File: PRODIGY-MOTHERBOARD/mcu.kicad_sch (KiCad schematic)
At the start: 19 parts, among them J1 USB_C_Receptacle, J2 Bus_M.2_Socket_B, SW1 SW_Push

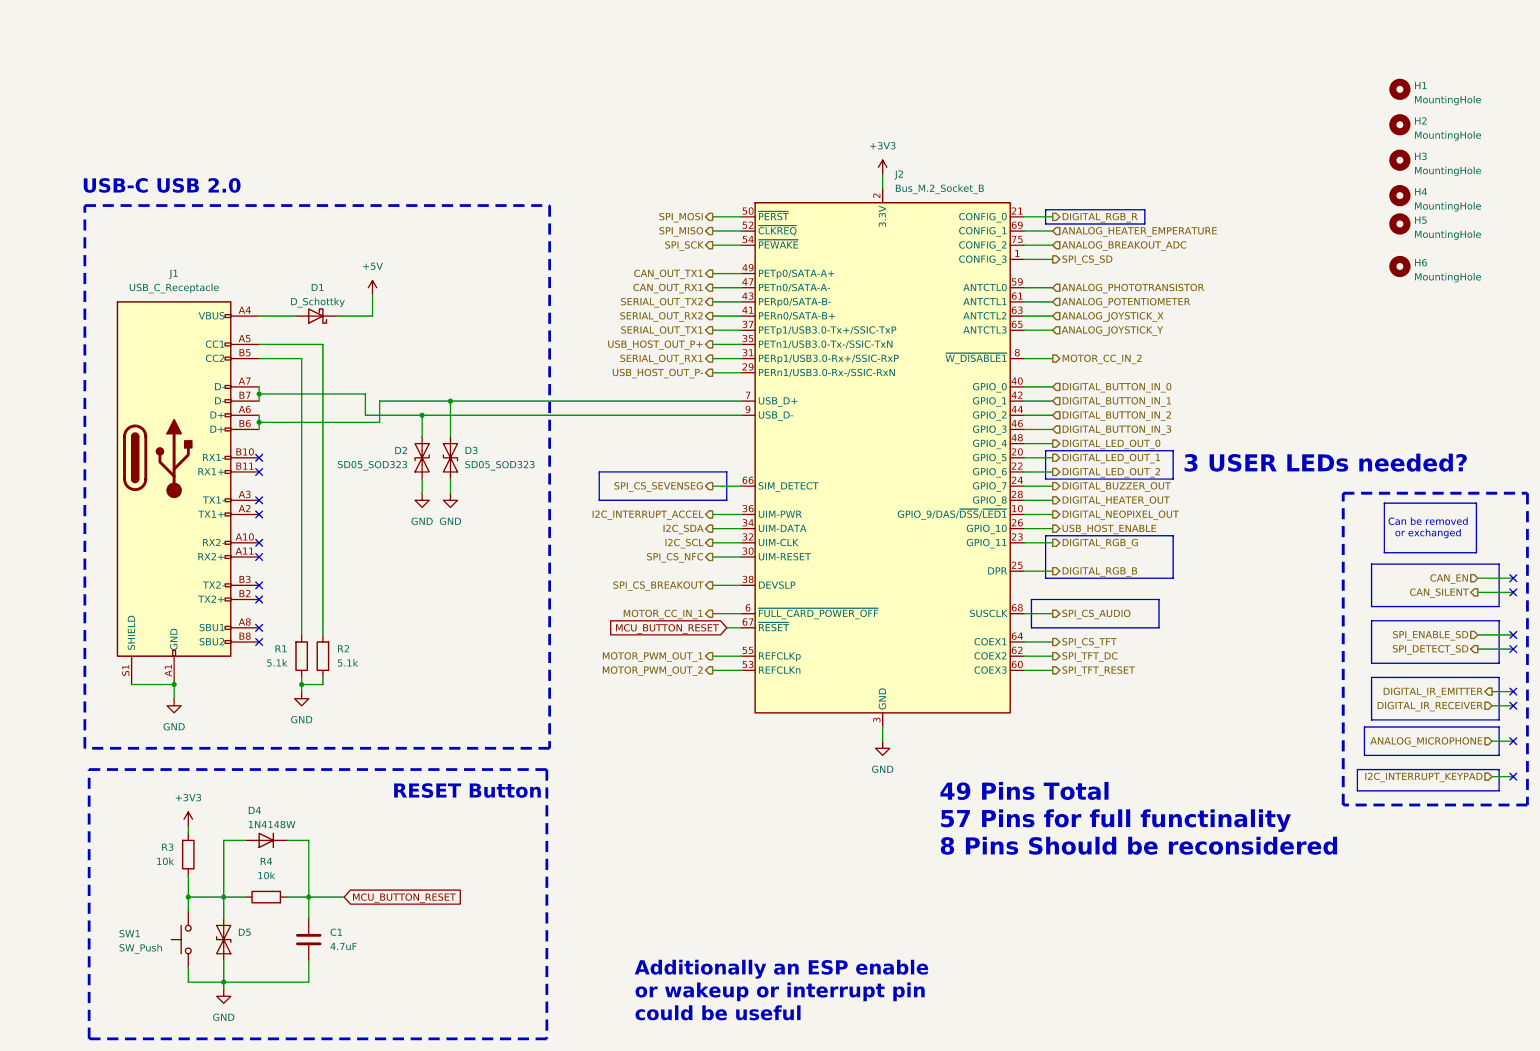
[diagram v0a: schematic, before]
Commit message: MCU schematic done. Started Analog design.
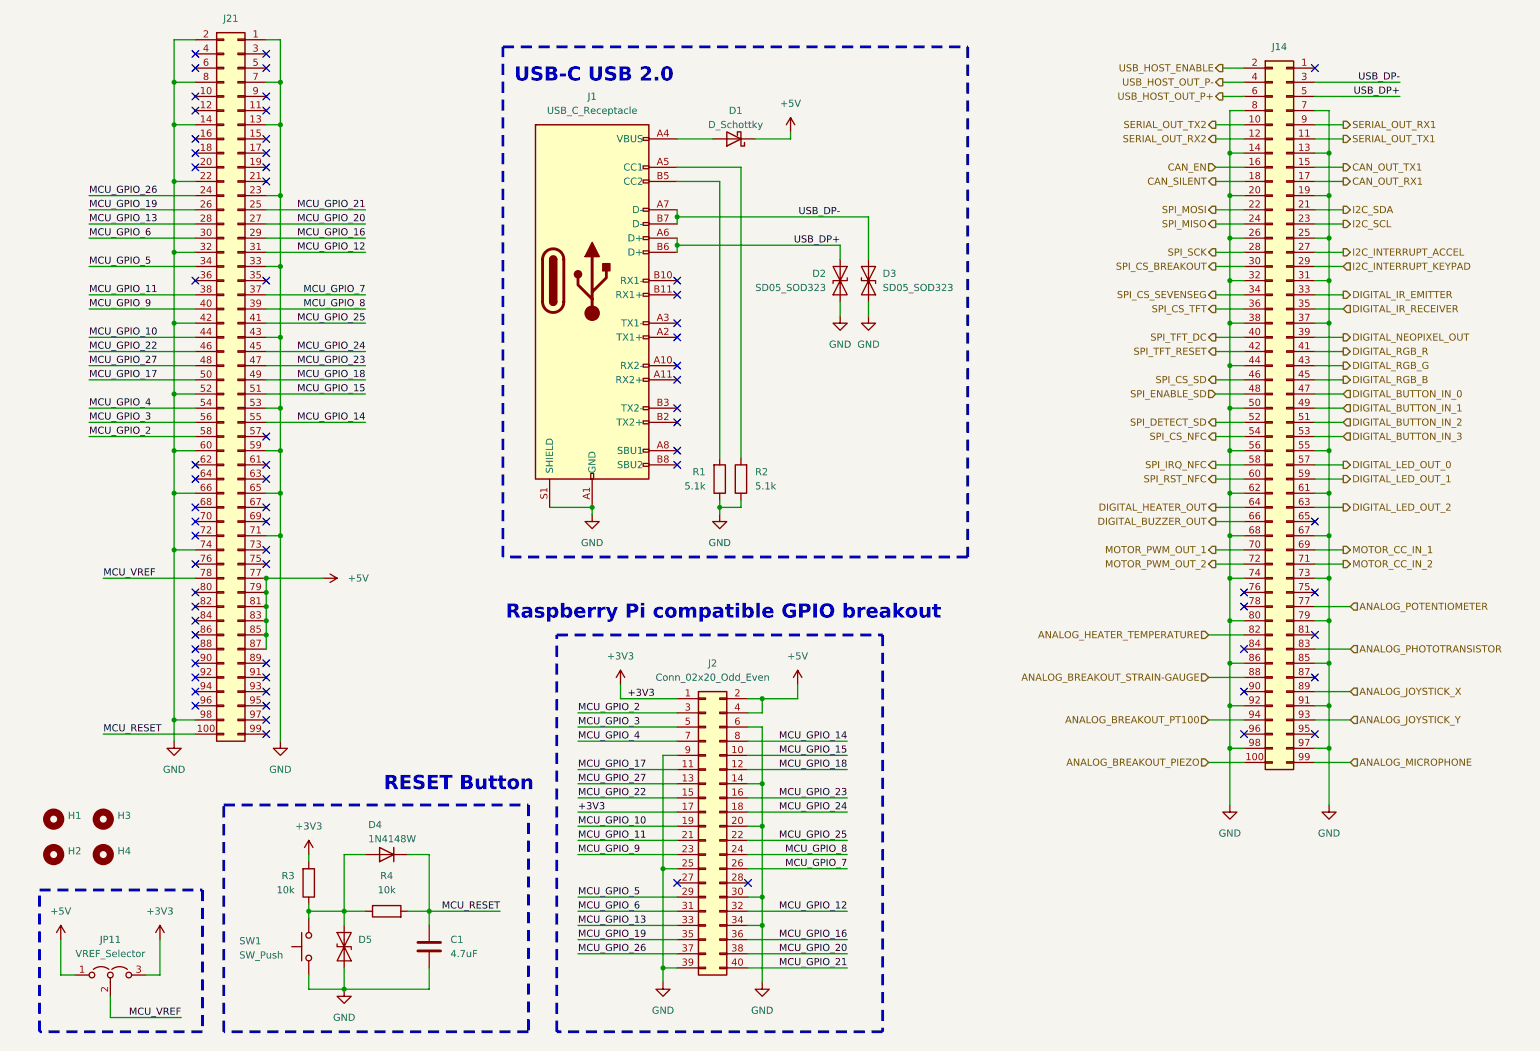
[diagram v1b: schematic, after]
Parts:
- removed H5, H6: MountingHole, MountingHole:MountingHole_3.2mm_M3_ISO7380_Pad_TopBottom, symbol Mechanical:MountingHole
- removed J2: Bus_M.2_Socket_B, symbol Connector:Bus_M.2_Socket_B
- added J14, J21: ~, symbol 2x50_generic_connector:2x50_Odd-Even
- added J2: Conn_02x20_Odd_Even, Connector_PinHeader_2.54mm:PinHeader_2x20_P2.54mm_Horizontal, symbol Connector_Generic:Conn_02x20_Odd_Even
- added JP11: VREF_Selector, symbol Jumper:Jumper_3_Open
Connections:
- net +3V3: now also J2.1 (Pin_1), J2.17 (Pin_17), JP11.3 (B)
- net +5V: now also J2.2 (Pin_2), J2.4 (Pin_4), J21.77, J21.79, J21.81, J21.83, J21.85, J21.87, JP11.1 (A)
- net ANALOG_JOYSTICK_X: now also J14.89
- net ANALOG_JOYSTICK_Y: now also J14.93
- net ANALOG_MICROPHONE: now also J14.99
- net ANALOG_PHOTOTRANSISTOR: now also J14.83
- net ANALOG_POTENTIOMETER: now also J14.77
- net CAN_EN: now also J14.16
- net CAN_OUT_RX1: now also J14.17
- net CAN_OUT_TX1: now also J14.15
- net CAN_SILENT: now also J14.18
- net DIGITAL_BUTTON_IN_0: now also J14.47
- net DIGITAL_BUTTON_IN_1: now also J14.49
- net DIGITAL_BUTTON_IN_2: now also J14.51
- net DIGITAL_BUTTON_IN_3: now also J14.53
- net DIGITAL_BUZZER_OUT: now also J14.66
- net DIGITAL_HEATER_OUT: now also J14.64
- net DIGITAL_IR_EMITTER: now also J14.33
- net DIGITAL_IR_RECEIVER: now also J14.35
- net DIGITAL_LED_OUT_0: now also J14.57
- net DIGITAL_LED_OUT_1: now also J14.59
- net DIGITAL_LED_OUT_2: now also J14.63
- net DIGITAL_NEOPIXEL_OUT: now also J14.39
- net DIGITAL_RGB_B: now also J14.45
- net DIGITAL_RGB_G: now also J14.43
- net DIGITAL_RGB_R: now also J14.41
- net GND: now also J14.13, J14.14, J14.19, J14.20, J14.25, J14.26, J14.31, J14.32, J14.37, J14.38, J14.44, J14.50, J14.55, J14.56, J14.61, J14.62, J14.67, J14.68, J14.7, J14.73, J14.74, J14.79, J14.8, J14.80, J14.85, J14.86, J14.91, J14.92, J14.97, J14.98, J2.14 (Pin_14), J2.20 (Pin_20), J2.25 (Pin_25), J2.30 (Pin_30), J2.34 (Pin_34), J2.39 (Pin_39), J2.6 (Pin_6), J2.9 (Pin_9), J21.1, J21.13, J21.14, J21.2, J21.22, J21.23, J21.32, J21.33, J21.42, J21.43, J21.52, J21.53, J21.59, J21.60, J21.65, J21.66, J21.7, J21.71, J21.74, J21.8, J21.98
- net I2C_INTERRUPT_ACCEL: now also J14.27
- net I2C_INTERRUPT_KEYPAD: now also J14.29
- net I2C_SCL: now also J14.23
- net I2C_SDA: now also J14.21
- net MOTOR_CC_IN_1: now also J14.69
- net MOTOR_CC_IN_2: now also J14.71
- net MOTOR_PWM_OUT_1: now also J14.70
- net MOTOR_PWM_OUT_2: now also J14.72
- net SERIAL_OUT_RX1: now also J14.9
- net SERIAL_OUT_RX2: now also J14.12
- net SERIAL_OUT_TX1: now also J14.11
- net SERIAL_OUT_TX2: now also J14.10
- net SPI_CS_BREAKOUT: now also J14.30
- net SPI_CS_NFC: now also J14.54
- net SPI_CS_SD: now also J14.46
- net SPI_CS_SEVENSEG: now also J14.34
- net SPI_CS_TFT: now also J14.36
- net SPI_DETECT_SD: now also J14.52
- net SPI_ENABLE_SD: now also J14.48
- net SPI_MISO: now also J14.24
- net SPI_MOSI: now also J14.22
- net SPI_SCK: now also J14.28
- net SPI_TFT_DC: now also J14.40
- net SPI_TFT_RESET: now also J14.42
- net USB_HOST_ENABLE: now also J14.2
- net USB_HOST_OUT_P+: now also J14.6
- net USB_HOST_OUT_P-: now also J14.4
- net USB_DP-: now reaches J1.A7 (D-), J1.B7 (D-)
- net USB_DP-: now also D3.2 (A2), J14.3; no longer D2.2 (A2)
- net USB_DP+: now reaches J1.A6 (D+), J1.B6 (D+)
- net USB_DP+: now also D2.2 (A2), J14.5; no longer D3.2 (A2)
- net MCU_BUTTON_RESET renamed MCU_RESET
- net MCU_RESET: now also J21.100
- new net ANALOG_BREAKOUT_PIEZO: J14.100
- new net ANALOG_BREAKOUT_PT100: J14.94
- new net ANALOG_BREAKOUT_STRAIN-GAUGE: J14.88
- new net ANALOG_HEATER_TEMPERATURE: J14.82
- new net MCU_GPIO_10: J2.19 (Pin_19), J21.44
- new net MCU_GPIO_11: J2.21 (Pin_21), J21.38
- new net MCU_GPIO_12: J2.32 (Pin_32), J21.31
- new net MCU_GPIO_13: J2.33 (Pin_33), J21.28
- new net MCU_GPIO_14: J2.8 (Pin_8), J21.55
- new net MCU_GPIO_15: J2.10 (Pin_10), J21.51
- new net MCU_GPIO_16: J2.36 (Pin_36), J21.29
- new net MCU_GPIO_17: J2.11 (Pin_11), J21.50
- new net MCU_GPIO_18: J2.12 (Pin_12), J21.49
- new net MCU_GPIO_19: J2.35 (Pin_35), J21.26
- new net MCU_GPIO_2: J2.3 (Pin_3), J21.58
- new net MCU_GPIO_20: J2.38 (Pin_38), J21.27
- new net MCU_GPIO_21: J2.40 (Pin_40), J21.25
- new net MCU_GPIO_22: J2.15 (Pin_15), J21.46
- new net MCU_GPIO_23: J2.16 (Pin_16), J21.47
- new net MCU_GPIO_24: J2.18 (Pin_18), J21.45
- new net MCU_GPIO_25: J2.22 (Pin_22), J21.41
- new net MCU_GPIO_26: J2.37 (Pin_37), J21.24
- new net MCU_GPIO_27: J2.13 (Pin_13), J21.48
- new net MCU_GPIO_3: J2.5 (Pin_5), J21.56
- new net MCU_GPIO_4: J2.7 (Pin_7), J21.54
- new net MCU_GPIO_5: J2.29 (Pin_29), J21.34
- new net MCU_GPIO_6: J2.31 (Pin_31), J21.30
- new net MCU_GPIO_7: J2.26 (Pin_26), J21.37
- new net MCU_GPIO_8: J2.24 (Pin_24), J21.39
- new net MCU_GPIO_9: J2.23 (Pin_23), J21.40
- new net MCU_VREF: J21.78, JP11.2 (C)
- new net SPI_IRQ_NFC: J14.58
- new net SPI_RST_NFC: J14.60
- no-connect marks 18 -> 68
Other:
- note added: "Raspberry Pi compatible GPIO breakout"
- note removed: "3 USER LEDs needed?"
- note removed: "49 Pins Total 57 Pins for full functinality 8 Pins Should be reconsidered"
- note removed: "Additionally an ESP enable or wakeup or interrupt pin could be useful"
- note removed: "Can be removed or exchanged"
- moved on the sheet: C1, D1, D2, D3, D4, D5, H1, J1, R1, R2, R3, R4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

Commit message: Finished v0.1 schematic.
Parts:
- removed H1, H2, H3, H4: MountingHole, MountingHole:MountingHole_3.2mm_M3_ISO7380_Pad_TopBottom, symbol Mechanical:MountingHole
- added FID7, FID8: Fiducial, symbol Mechanical:Fiducial
- added H5, H6, H7, H8: MountingHole, MountingHole:MountingHole_3.2mm_M3_ISO7380_Pad_TopBottom, symbol Mechanical:MountingHole
- J1: renamed from J21; value ~ -> DF40C-100DS-0.4V(51)
- J2: renamed from J1; footprint (none) -> Connector_USB:USB_C_Receptacle_G-Switch_GT-USB-7025
- J4: renamed from J14; value ~ -> DF40C-100DS-0.4V(51)
- renumbered D5 to D1, D4 to D2, D1 to D3, D2 to D4, D3 to D5, J2 to J3, JP11 to JP1, R3 to R1, R4 to R2, R1 to R3, R2 to R4
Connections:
- net ANALOG_BREAKOUT_STRAIN-GAUGE is gone; now on net ANALOG_HEATER_TEMPERATURE: J4.88
- net ANALOG_HEATER_TEMPERATURE: no longer J4.82
- net ANALOG_JOYSTICK_X: now also J4.87; no longer J4.89
- net ANALOG_PHOTOTRANSISTOR: now also J4.81; no longer J4.83
- net ANALOG_POTENTIOMETER: now also J4.82; no longer J4.77
- no-connect marks 68 -> 69
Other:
- moved on the sheet: J1, JP1

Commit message: MBT Schematic improved
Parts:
- added JP12: Vout_select, symbol Jumper:Jumper_3_Bridged12
- added TP15: ~, TestPoint:TestPoint_Pad_D3.0mm, symbol Connector:TestPoint
- J3: footprint Connector_PinHeader_2.54mm:PinHeader_2x20_P2.54mm_Horizontal -> Connector_IDC:IDC-Header_2x20_P2.54mm_Horizontal
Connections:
- net SPI_CS_SD is gone; now on net SPI_CS_NFC: J4.46
- net SPI_DETECT_SD is gone; now on net SPI_RST_NFC: J4.52
- net SPI_ENABLE_SD is gone; now on net SPI_IRQ_NFC: J4.48
- net +3V3: now also J1.84, J1.86, JP12.1 (A)
- net DIGITAL_BUZZER_OUT: now also J4.60; no longer J4.66
- net DIGITAL_HEATER_OUT: now also J4.54; no longer J4.64
- net DIGITAL_LED_OUT_2: now also J4.58; no longer J4.63
- net MCU_VREF: now also TP15.1
- net MOTOR_CC_IN_1: now also J4.65; no longer J4.69
- net MOTOR_CC_IN_2: now also J4.66; no longer J4.71
- net MOTOR_PWM_OUT_1: now also J4.63; no longer J4.70
- net MOTOR_PWM_OUT_2: now also J4.64; no longer J4.72
- net SPI_CS_NFC: no longer J4.54
- net SPI_IRQ_NFC: no longer J4.58
- net SPI_RST_NFC: no longer J4.60
- net SD_CLK: now reaches J1.57
- net SD_DAT3: now reaches J1.61
- net SD_CMD: now reaches J1.62
- net SD_DAT0: now reaches J1.63
- net SD_DAT1: now reaches J1.67
- net SD_DAT2: now reaches J1.69
- net SD_Enable: now reaches J1.75
- net SD_DET: now reaches J1.76
- net at J1.88: now also J1.90, JP12.2 (C)
- net USB_HOST_FAULT: now reaches J4.1
- new net +1V8: JP12.3 (B)
- no-connect marks 69 -> 59
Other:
- moved on the sheet: J1

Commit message: schematic v0.2 finalized
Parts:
- renumbered H5 to H6, H6 to H7, H7 to H8, H8 to H9, JP12 to JP2, TP15 to TP1
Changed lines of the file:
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@@
 		(dnp no)
 		(fields_autoplaced yes)
-		(property "Reference" "H8"
+		(property "Reference" "H9"
 			(at 41.91 165.735 0)
 			(effects
@@
 			(project "PRODIGY-MOTHERBOARD"
 				(path "/f1c25860-8989-4190-bd24-2491d23ca7d9/27fc7bb4-2bbd-477b-b6e3-e07582947566"
-					(reference "H8")
+					(reference "H9")
 					(unit 1)
 				)
@@
 		(dnp no)
 		(fields_autoplaced yes)
-		(property "Reference" "H7"
+		(property "Reference" "H8"
 			(at 41.91 159.385 0)
 			(effects
@@
 			(project "PRODIGY-MOTHERBOARD"
 				(path "/f1c25860-8989-4190-bd24-2491d23ca7d9/27fc7bb4-2bbd-477b-b6e3-e07582947566"
-					(reference "H7")
+					(reference "H8")
 					(unit 1)
 				)
@@
 		(dnp no)
 		(fields_autoplaced yes)
-		(property "Reference" "#PWR014"
+		(property "Reference" "#PWR016"
 			(at 151.13 137.16 0)
 			(effects
@@
 			(project "PRODIGY-MOTHERBOARD"
 				(path "/f1c25860-8989-4190-bd24-2491d23ca7d9/27fc7bb4-2bbd-477b-b6e3-e07582947566"
-					(reference "#PWR014")
+					(reference "#PWR016")
 					(unit 1)
 				)
@@
 		(on_board yes)
 		(dnp no)
-		(property "Reference" "#PWR06"
+		(property "Reference" "#PWR08"
 			(at 66.04 116.84 0)
 			(effects
@@
 			(project "PRODIGY-MOTHERBOARD"
 				(path "/f1c25860-8989-4190-bd24-2491d23ca7d9/27fc7bb4-2bbd-477b-b6e3-e07582947566"
-					(reference "#PWR06")
+					(reference "#PWR08")
 					(unit 1)
 				)
@@
 		(dnp no)
 		(fields_autoplaced yes)
-		(property "Reference" "#PWR012"
+		(property "Reference" "#PWR014"
 			(at 144.78 193.04 0)
 			(effects
@@
 			(project "PRODIGY-MOTHERBOARD"
 				(path "/f1c25860-8989-4190-bd24-2491d23ca7d9/27fc7bb4-2bbd-477b-b6e3-e07582947566"
-					(reference "#PWR012")
+					(reference "#PWR014")
 					(unit 1)
 				)
@@
 		(dnp no)
 		(fields_autoplaced yes)
-		(property "Reference" "#PWR09"
+		(property "Reference" "#PWR011"
 			(at 119.38 137.16 0)
 			(effects
@@
 			(project "PRODIGY-MOTHERBOARD"
 				(path "/f1c25860-8989-4190-bd24-2491d23ca7d9/27fc7bb4-2bbd-477b-b6e3-e07582947566"
-					(reference "#PWR09")
+					(reference "#PWR011")
 					(unit 1)
 				)
@@
 		(dnp no)
 		(fields_autoplaced yes)
-		(property "Reference" "#PWR0248"
+		(property "Reference" "#PWR02"
 			(at 34.29 124.46 0)
 			(effects
@@
 			(project "PRODIGY-MOTHERBOARD"
 				(path "/f1c25860-8989-4190-bd24-2491d23ca7d9/27fc7bb4-2bbd-477b-b6e3-e07582947566"
-					(reference "#PWR0248")
+					(reference "#PWR02")
 					(unit 1)
 				)
@@
 		(dnp no)
 		(fields_autoplaced yes)
-		(property "Reference" "H6"
+		(property "Reference" "H7"
 			(at 33.02 165.735 0)
 			(effects
@@
 			(project "PRODIGY-MOTHERBOARD"
 				(path "/f1c25860-8989-4190-bd24-2491d23ca7d9/27fc7bb4-2bbd-477b-b6e3-e07582947566"
-					(reference "H6")
+					(reference "H7")
 					(unit 1)
 				)
@@
 		(dnp no)
 		(fields_autoplaced yes)
-		(property "Reference" "#PWR015"
+		(property "Reference" "#PWR017"
 			(at 158.75 73.66 0)
 			(effects
@@
 			(project "PRODIGY-MOTHERBOARD"
 				(path "/f1c25860-8989-4190-bd24-2491d23ca7d9/27fc7bb4-2bbd-477b-b6e3-e07582947566"
-					(reference "#PWR015")
+					(reference "#PWR017")
 					(unit 1)
 				)
@@
 		(dnp no)
 		(fields_autoplaced yes)
-		(property "Reference" "#PWR016"
+		(property "Reference" "#PWR018"
 			(at 163.83 73.66 0)
 			(effects
@@
 			(project "PRODIGY-MOTHERBOARD"
 				(path "/f1c25860-8989-4190-bd24-2491d23ca7d9/27fc7bb4-2bbd-477b-b6e3-e07582947566"
-					(reference "#PWR016")
+					(reference "#PWR018")
 					(unit 1)
 				)
@@
 		(dnp no)
 		(fields_autoplaced yes)
-		(property "Reference" "#PWR07"
+		(property "Reference" "#PWR09"
 			(at 69.85 194.31 0)
 			(effects
@@
 			(project "PRODIGY-MOTHERBOARD"
 				(path "/f1c25860-8989-4190-bd24-2491d23ca7d9/27fc7bb4-2bbd-477b-b6e3-e07582947566"
-					(reference "#PWR07")
+					(reference "#PWR09")
 					(unit 1)
 				)
@@
 		(dnp no)
 		(fields_autoplaced yes)
-		(property "Reference" "#PWR011"
+		(property "Reference" "#PWR013"
 			(at 137.16 109.22 0)
 			(effects
@@
 			(project "PRODIGY-MOTHERBOARD"
 				(path "/f1c25860-8989-4190-bd24-2491d23ca7d9/27fc7bb4-2bbd-477b-b6e3-e07582947566"
-					(reference "#PWR011")
+					(reference "#PWR013")
 					(unit 1)
 				)
@@
 		(dnp no)
 		(fields_autoplaced yes)
-		(property "Reference" "#PWR010"
+		(property "Reference" "#PWR012"
 			(at 127 193.04 0)
 			(effects
@@
 			(project "PRODIGY-MOTHERBOARD"
 				(path "/f1c25860-8989-4190-bd24-2491d23ca7d9/27fc7bb4-2bbd-477b-b6e3-e07582947566"
-					(reference "#PWR010")
+					(reference "#PWR012")
 					(unit 1)
 				)
@@
 		(dnp no)
 		(fields_autoplaced yes)
-		(property "Reference" "#PWR05"
+		(property "Reference" "#PWR07"
 			(at 63.5 167.64 0)
 			(effects
@@
 			(project "PRODIGY-MOTHERBOARD"
 				(path "/f1c25860-8989-4190-bd24-2491d23ca7d9/27fc7bb4-2bbd-477b-b6e3-e07582947566"
-					(reference "#PWR05")
+					(reference "#PWR07")
 					(unit 1)
 				)
@@
 		(dnp no)
 		(fields_autoplaced yes)
-		(property "Reference" "#PWR08"
+		(property "Reference" "#PWR010"
 			(at 114.3 109.22 0)
 			(effects
@@
 			(project "PRODIGY-MOTHERBOARD"
 				(path "/f1c25860-8989-4190-bd24-2491d23ca7d9/27fc7bb4-2bbd-477b-b6e3-e07582947566"
-					(reference "#PWR08")
+					(reference "#PWR010")
 					(unit 1)
 				)
@@
 		(dnp no)
 		(fields_autoplaced yes)
-		(property "Reference" "JP12"
+		(property "Reference" "JP2"
 			(at 29.21 129.5399 90)
 			(effects
@@
 			(project ""
 				(path "/f1c25860-8989-4190-bd24-2491d23ca7d9/27fc7bb4-2bbd-477b-b6e3-e07582947566"
-					(reference "JP12")
+					(reference "JP2")
 					(unit 1)
 				)
@@
 		(dnp no)
 		(fields_autoplaced yes)
-		(property "Reference" "H5"
+		(property "Reference" "H6"
 			(at 33.02 159.385 0)
 			(effects
@@
 			(project "PRODIGY-MOTHERBOARD"
 				(path "/f1c25860-8989-4190-bd24-2491d23ca7d9/27fc7bb4-2bbd-477b-b6e3-e07582947566"
-					(reference "H5")
+					(reference "H6")
 					(unit 1)
 				)
@@
 		(dnp no)
 		(fields_autoplaced yes)
-		(property "Reference" "#PWR03"
+		(property "Reference" "#PWR05"
 			(at 43.18 152.4 0)
 			(effects
@@
 			(project "PRODIGY-MOTHERBOARD"
 				(path "/f1c25860-8989-4190-bd24-2491d23ca7d9/27fc7bb4-2bbd-477b-b6e3-e07582947566"
-					(reference "#PWR03")
+					(reference "#PWR05")
 					(unit 1)
 				)
@@
 		(dnp no)
 		(fields_autoplaced yes)
-		(property "Reference" "#PWR018"
+		(property "Reference" "#PWR020"
 			(at 246.38 161.29 0)
 			(effects
@@
 			(project "PRODIGY-MOTHERBOARD"
 				(path "/f1c25860-8989-4190-bd24-2491d23ca7d9/27fc7bb4-2bbd-477b-b6e3-e07582947566"
-					(reference "#PWR018")
+					(reference "#PWR020")
 					(unit 1)
 				)
@@
 		(dnp no)
 		(fields_autoplaced yes)
-		(property "Reference" "#PWR04"
+		(property "Reference" "#PWR06"
 			(at 62.23 152.4 0)
 			(effects
@@
 			(project "PRODIGY-MOTHERBOARD"
 				(path "/f1c25860-8989-4190-bd24-2491d23ca7d9/27fc7bb4-2bbd-477b-b6e3-e07582947566"
-					(reference "#PWR04")
+					(reference "#PWR06")
 					(unit 1)
 				)
@@
 		(dnp no)
 		(fields_autoplaced yes)
-		(property "Reference" "#PWR02"
+		(property "Reference" "#PWR04"
 			(at 36.83 181.61 0)
 			(effects
@@
 			(project "PRODIGY-MOTHERBOARD"
 				(path "/f1c25860-8989-4190-bd24-2491d23ca7d9/27fc7bb4-2bbd-477b-b6e3-e07582947566"
-					(reference "#PWR02")
+					(reference "#PWR04")
 					(unit 1)
 				)
@@
 		(dnp no)
 		(fields_autoplaced yes)
-		(property "Reference" "#PWR017"
+		(property "Reference" "#PWR019"
 			(at 228.6 161.29 0)
 			(effects
@@
 			(project "PRODIGY-MOTHERBOARD"
 				(path "/f1c25860-8989-4190-bd24-2491d23ca7d9/27fc7bb4-2bbd-477b-b6e3-e07582947566"
-					(reference "#PWR017")
+					(reference "#PWR019")
 					(unit 1)
 				)
@@
 		(on_board yes)
 		(dnp no)
-		(property "Reference" "TP15"
+		(property "Reference" "TP1"
 			(at 36.83 185.9279 0)
 			(effects
@@
 			(project "PRODIGY-MOTHERBOARD"
 				(path "/f1c25860-8989-4190-bd24-2491d23ca7d9/27fc7bb4-2bbd-477b-b6e3-e07582947566"
-					(reference "TP15")
+					(reference "TP1")
 					(unit 1)
 				)
@@
 		(dnp no)
 		(fields_autoplaced yes)
-		(property "Reference" "#PWR013"
+		(property "Reference" "#PWR015"
 			(at 149.86 38.1 0)
 			(effects
@@
 			(project "PRODIGY-MOTHERBOARD"
 				(path "/f1c25860-8989-4190-bd24-2491d23ca7d9/27fc7bb4-2bbd-477b-b6e3-e07582947566"
-					(reference "#PWR013")
+					(reference "#PWR015")
 					(unit 1)
 				)
@@
 		(dnp no)
 		(fields_autoplaced yes)
-		(property "Reference" "#PWR0249"
+		(property "Reference" "#PWR03"
 			(at 34.29 139.7 0)
 			(effects
@@
 			(project ""
 				(path "/f1c25860-8989-4190-bd24-2491d23ca7d9/27fc7bb4-2bbd-477b-b6e3-e07582947566"
-					(reference "#PWR0249")
+					(reference "#PWR03")
 					(unit 1)
 				)
